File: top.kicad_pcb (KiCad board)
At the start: 2 copper layers, 49.5 x 147.2 mm, 5 parts, among them J1 Conn_01x04, J3 Conn_01x02, J4 Conn_01x02, J5 Conn_01x02

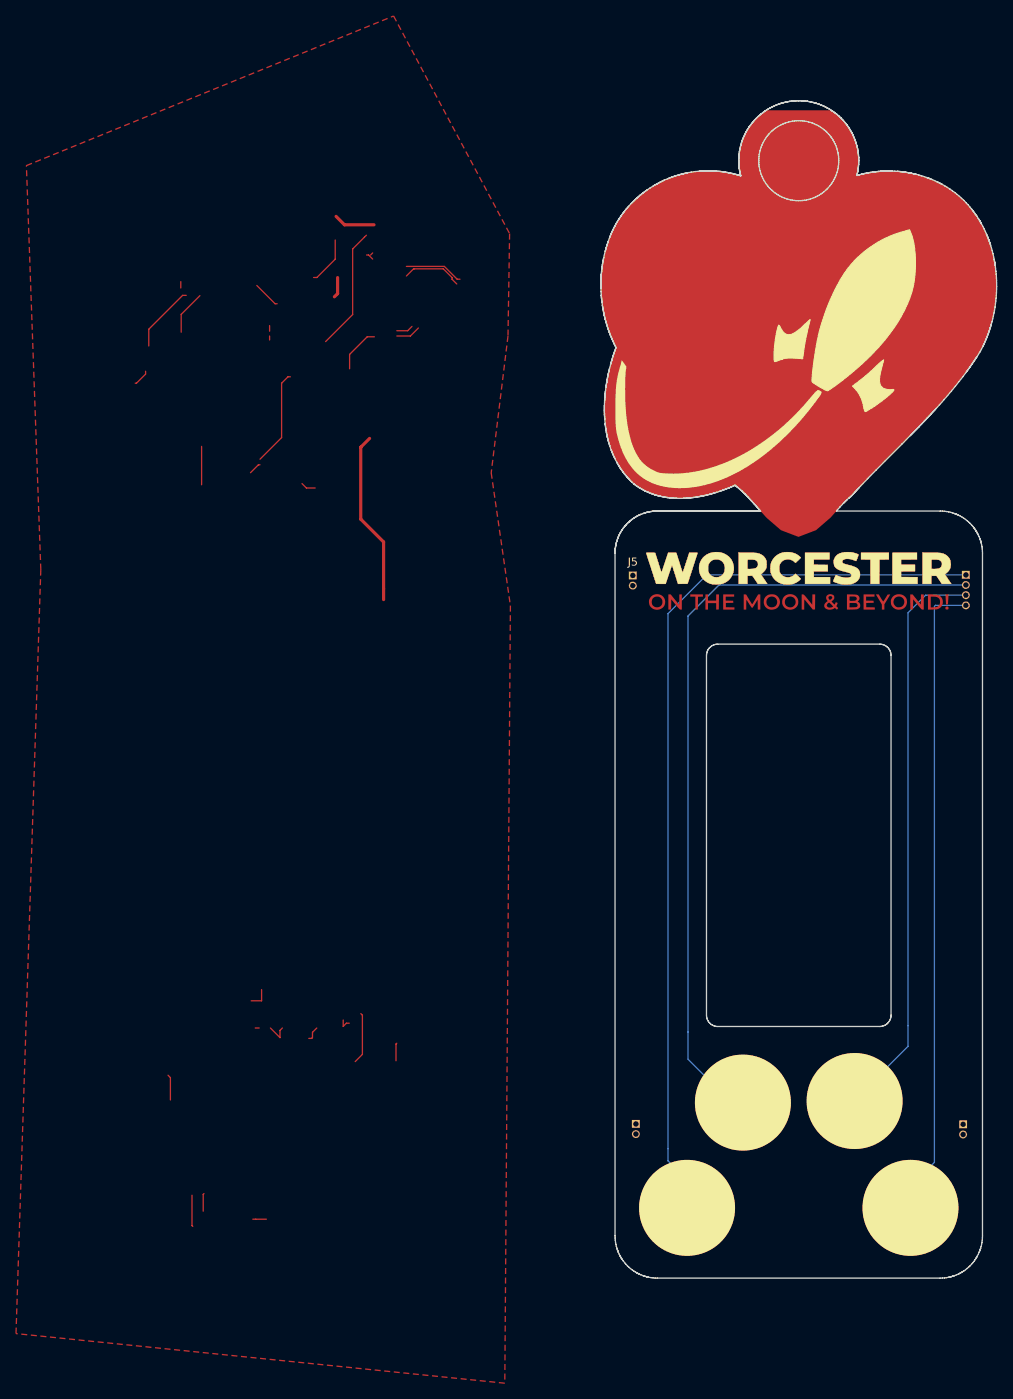
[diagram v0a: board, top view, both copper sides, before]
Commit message: removed extra pour
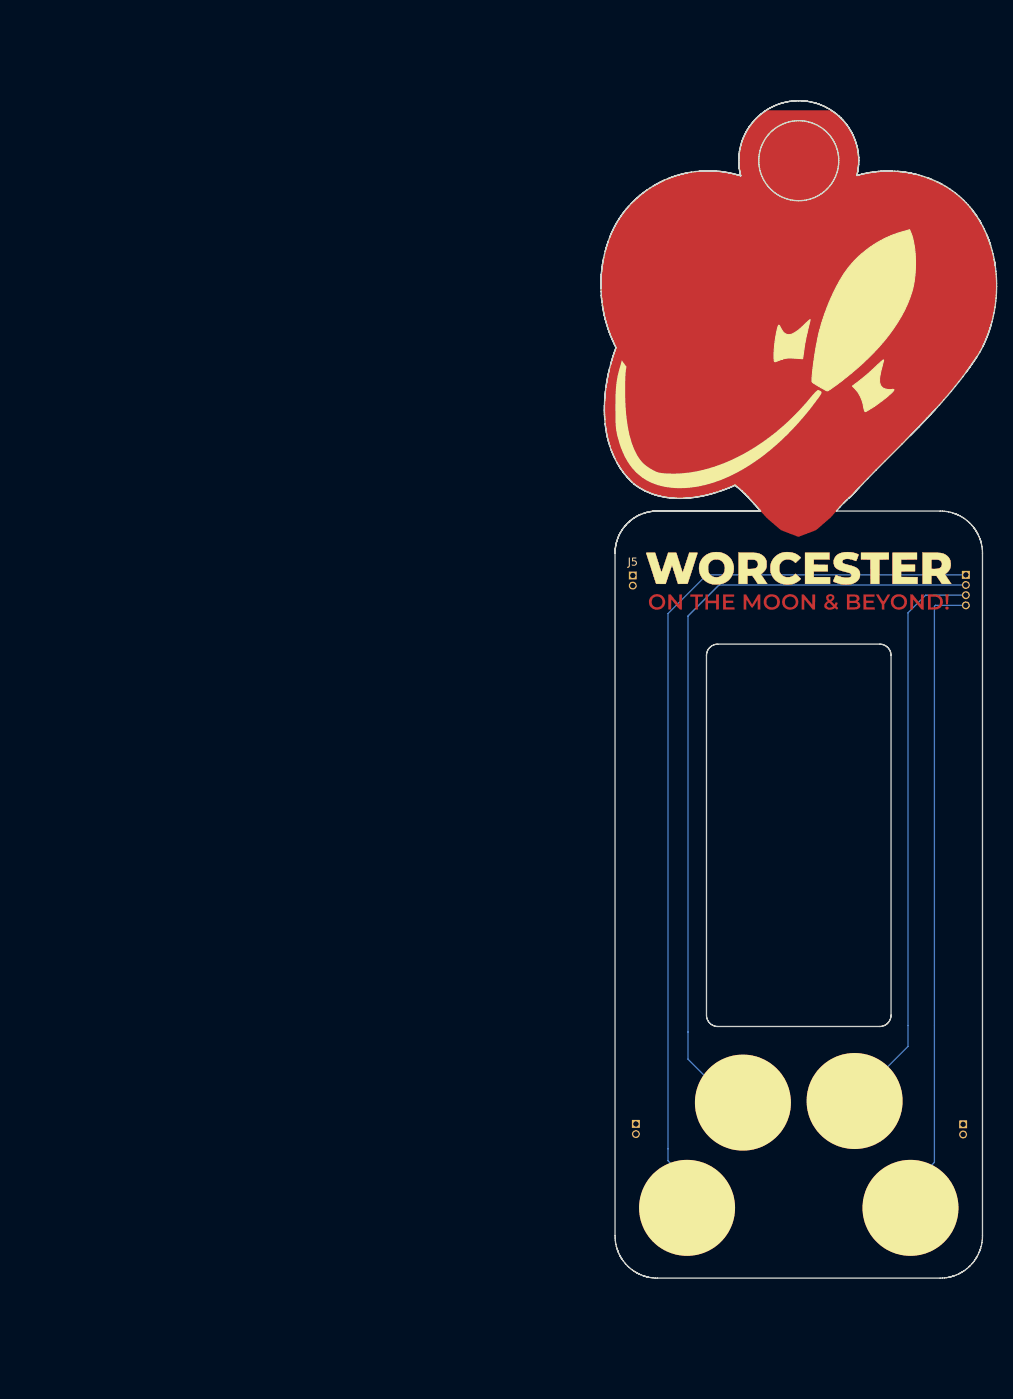
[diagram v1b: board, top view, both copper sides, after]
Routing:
- net +3V3: track 34.7 -> 0.00 mm
- net GND: track 21.1 -> 0.00 mm
- net INT: track 15.4 -> 0.00 mm
- net EINK_DC: track 12.0 -> 0.00 mm
- net EINK_MOSI: track 10.8 -> 0.00 mm
- net DTR: track 7.93 -> 0.00 mm
- net Net-(J2-Pad3): track 7.58 -> 0.00 mm
- net Net-(J2-Pad2): track 7.36 -> 0.00 mm
- net VGL: track 6.46 -> 0.00 mm
- net MISO: track 6.07 -> 0.00 mm
- net SDA: track 5.54 -> 0.00 mm
- net MMC_CS: track 4.80 -> 0.00 mm
- net EINK_SCLK: track 3.22 -> 0.00 mm
- net RTS: track 3.11 -> 0.00 mm
- net VGH: track 2.24 -> 0.00 mm
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- removed copper zone on F.Cu, net GND

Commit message: removed designators, more cosmetic fixes
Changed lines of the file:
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@@
     (35 F.Paste user)
     (36 B.SilkS user)
-    (37 F.SilkS user hide)
+    (37 F.SilkS user)
     (38 B.Mask user)
     (39 F.Mask user)
@@
     (descr "Through hole straight pin header, 1x02, 1.27mm pitch, single row")
     (tags "Through hole pin header THT 1x02 1.27mm single row")
-    (fp_text reference J5 (at 0 1.695) (layer F.SilkS)
-      (effects (font (size 1 1) (thickness 0.15)))
+    (fp_text reference J5 (at 0 1.695) (layer B.SilkS)
+      (effects (font (size 1 1) (thickness 0.15)) (justify mirror))
     )
     (fp_text value Conn_01x02 (at 0 -2.965) (layer B.Fab)
